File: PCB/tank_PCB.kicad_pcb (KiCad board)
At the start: 2 copper layers, 49 x 91 mm, 64 parts, among them J1 TFT, J2 PTSA 1,5/ 2-3,5-Z, J3 PTSA 1,5/ 8-3,5-Z, J5 USB4110GFA, U1 ADS1115IDGS, U3 LM2735X (1.6MHz), U4 ESP32-C6-WROOM-1, U5 MCP1826S-3302E/DB

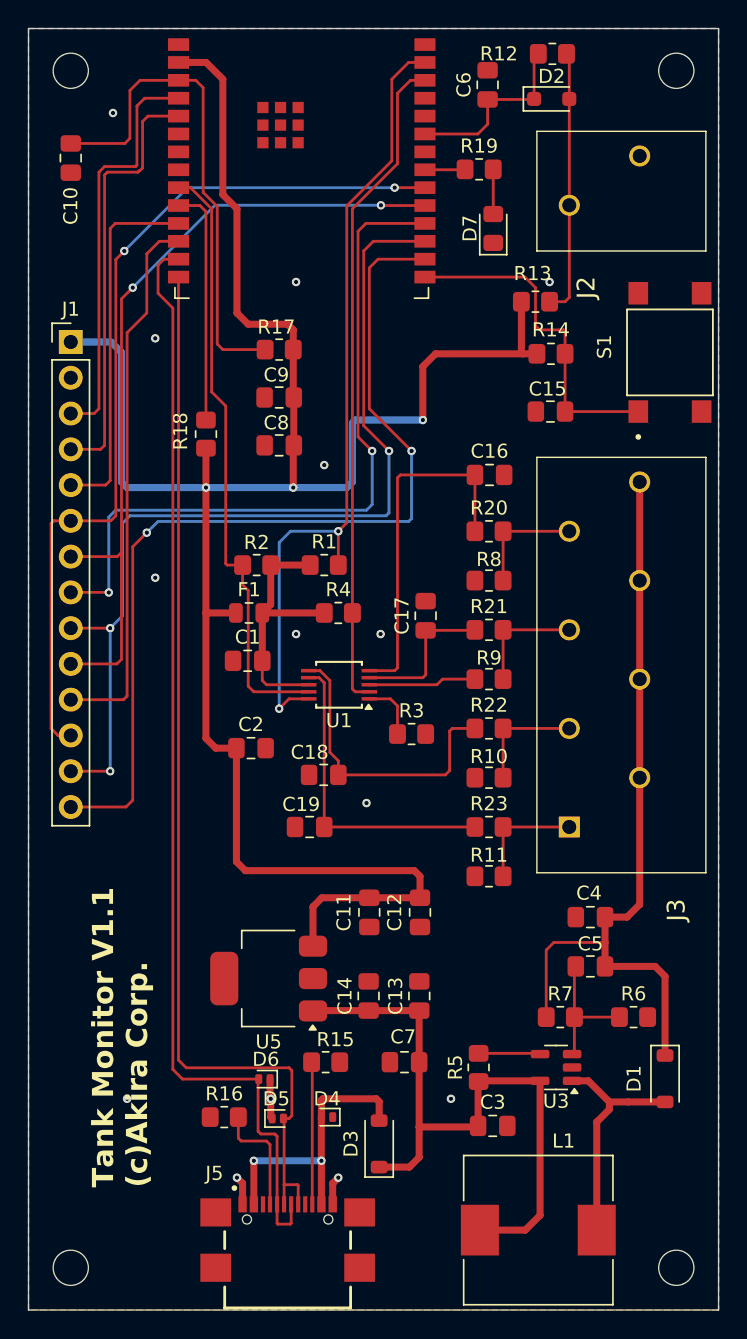
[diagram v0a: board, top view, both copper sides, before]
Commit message: updating PCB Kicad v9
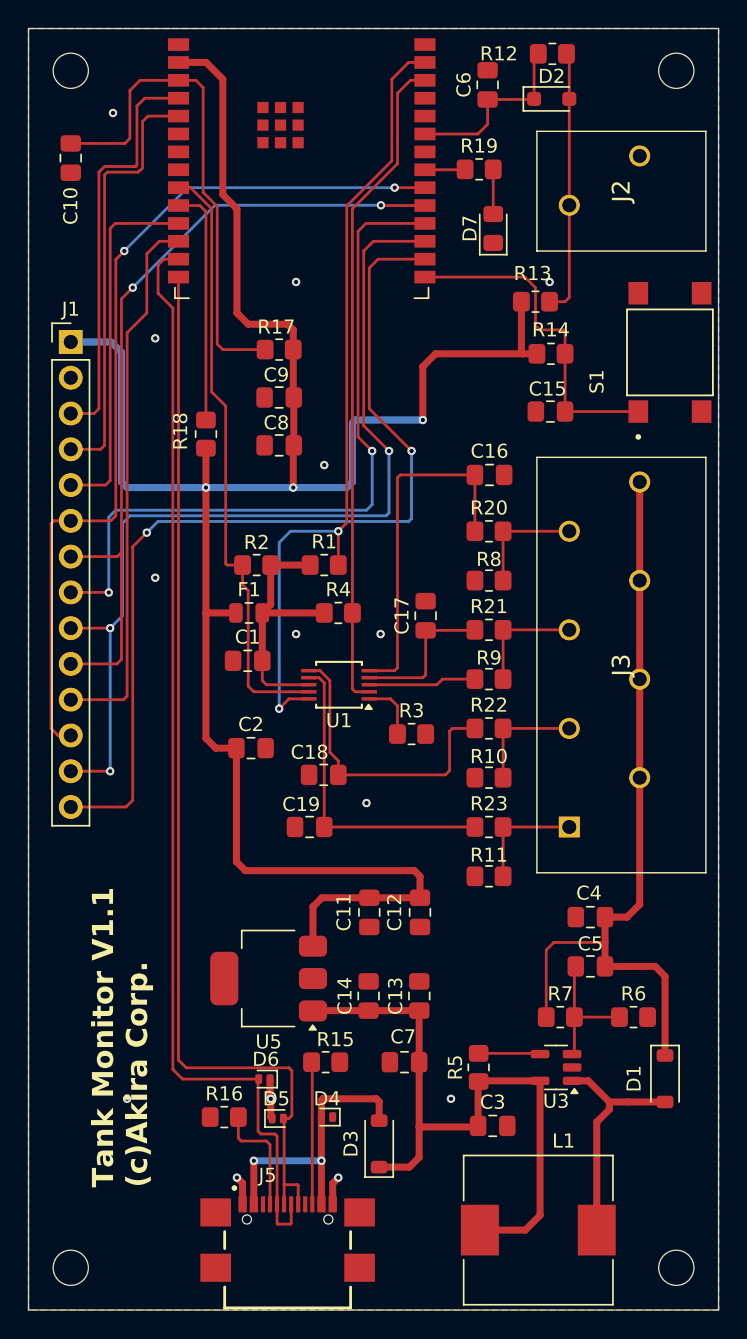
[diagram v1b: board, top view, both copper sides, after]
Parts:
- J2: footprint Phoenix Contact PTSA 2:1985195 -> zTankFootprints:Phoenix Contact PTSA 2
- J3: footprint Phoenix Contact PTSA 8:1985250 -> zTankFootprints:Phoenix Contact PTSA 8
- J5: footprint GCT-USB4110GFA:GCT_USB4110GFA -> zTankFootprints:GCT_USB4110GFA
- S1: footprint CUI switch:SW_TS07-667-30-BK-100-SMT-TR -> zTankFootprints:CUI switch SW_TS07-667-30-BK-100-SMT-TR

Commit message: Correcting PCB bug J3 pin 7 at GND
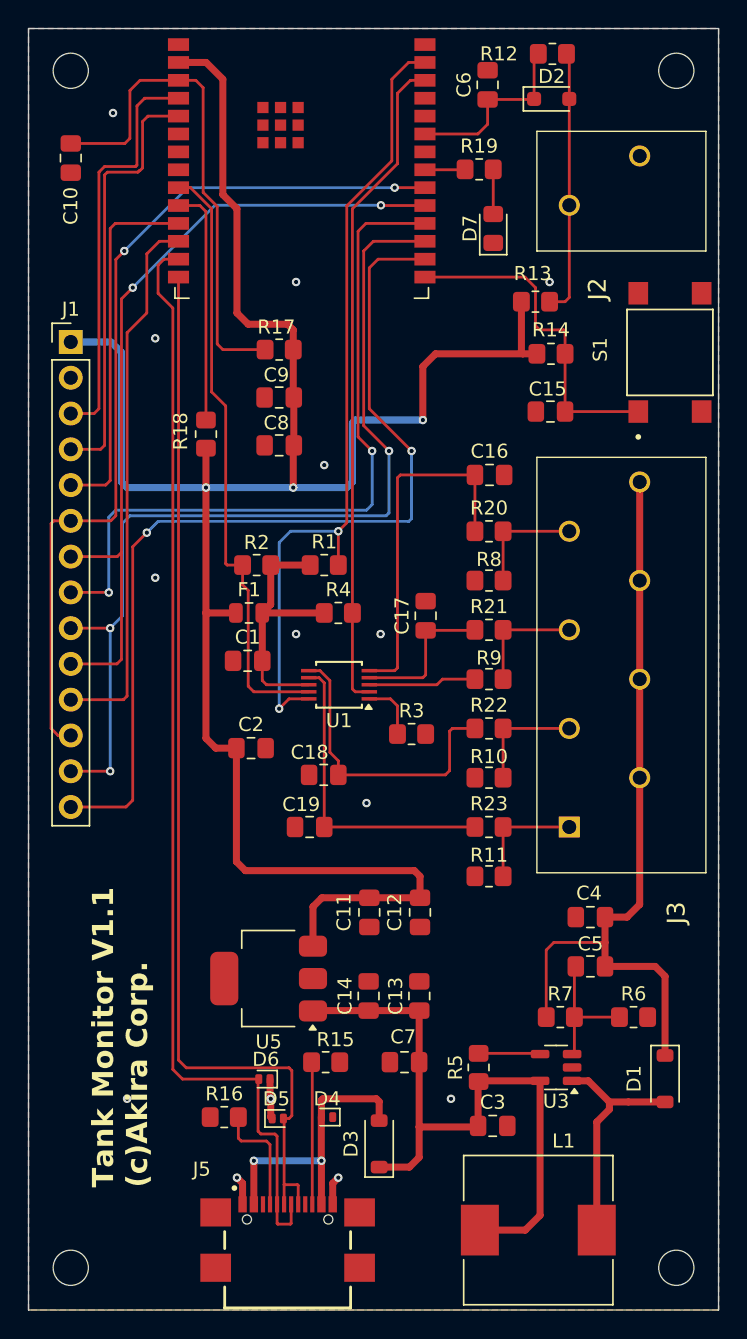
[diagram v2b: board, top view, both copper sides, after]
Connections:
- J3 pad 7: GND -> Net-(J3-Pad7)
- R20 pad 2: GND -> Net-(J3-Pad7)
- R8 pad 1: GND -> Net-(J3-Pad7)
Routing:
- net Net-(J3-Pad7): track 0.00 -> 8.20 mm
- net GND: track 23.1 -> 14.9 mm
